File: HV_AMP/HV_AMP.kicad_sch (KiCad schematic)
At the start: 54 parts, among them K1 G5V-2, Q1 BC546, Q3 BC549, Q4 BC546, U1 4N35, U2 TL072, U3 TL072, U4 TL072, U5 LM7815_TO220, U6 LM7915_TO220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

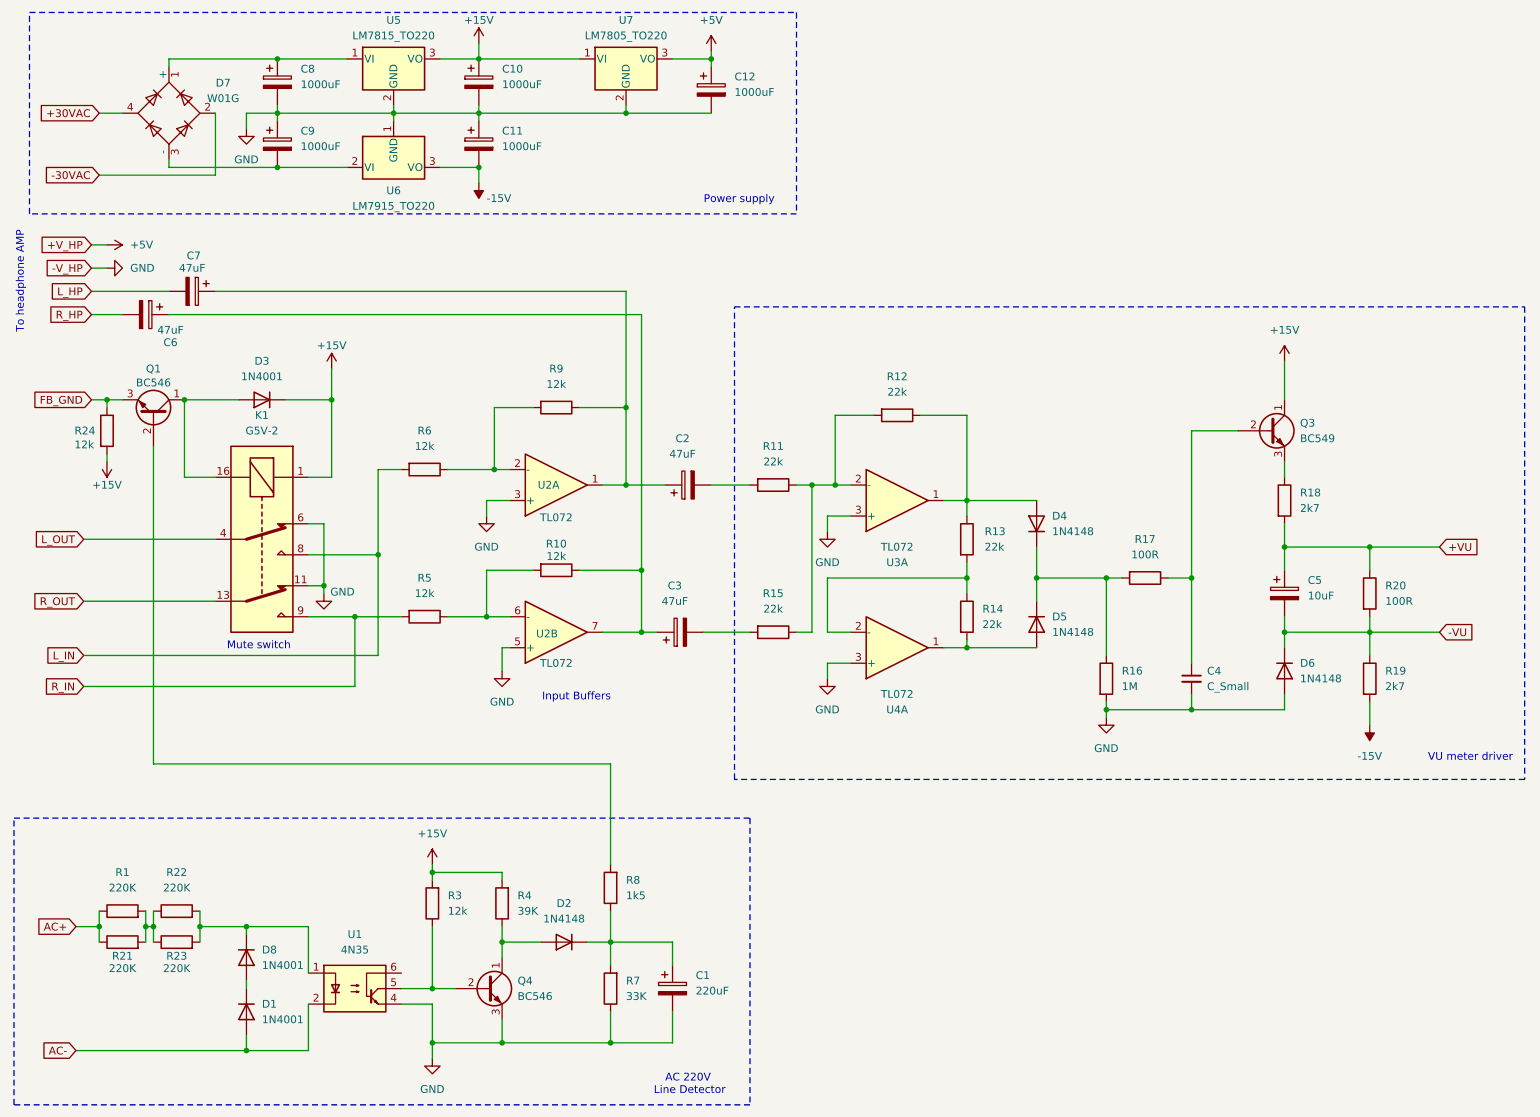
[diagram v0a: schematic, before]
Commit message: Fixing some circuit values for HV AMP
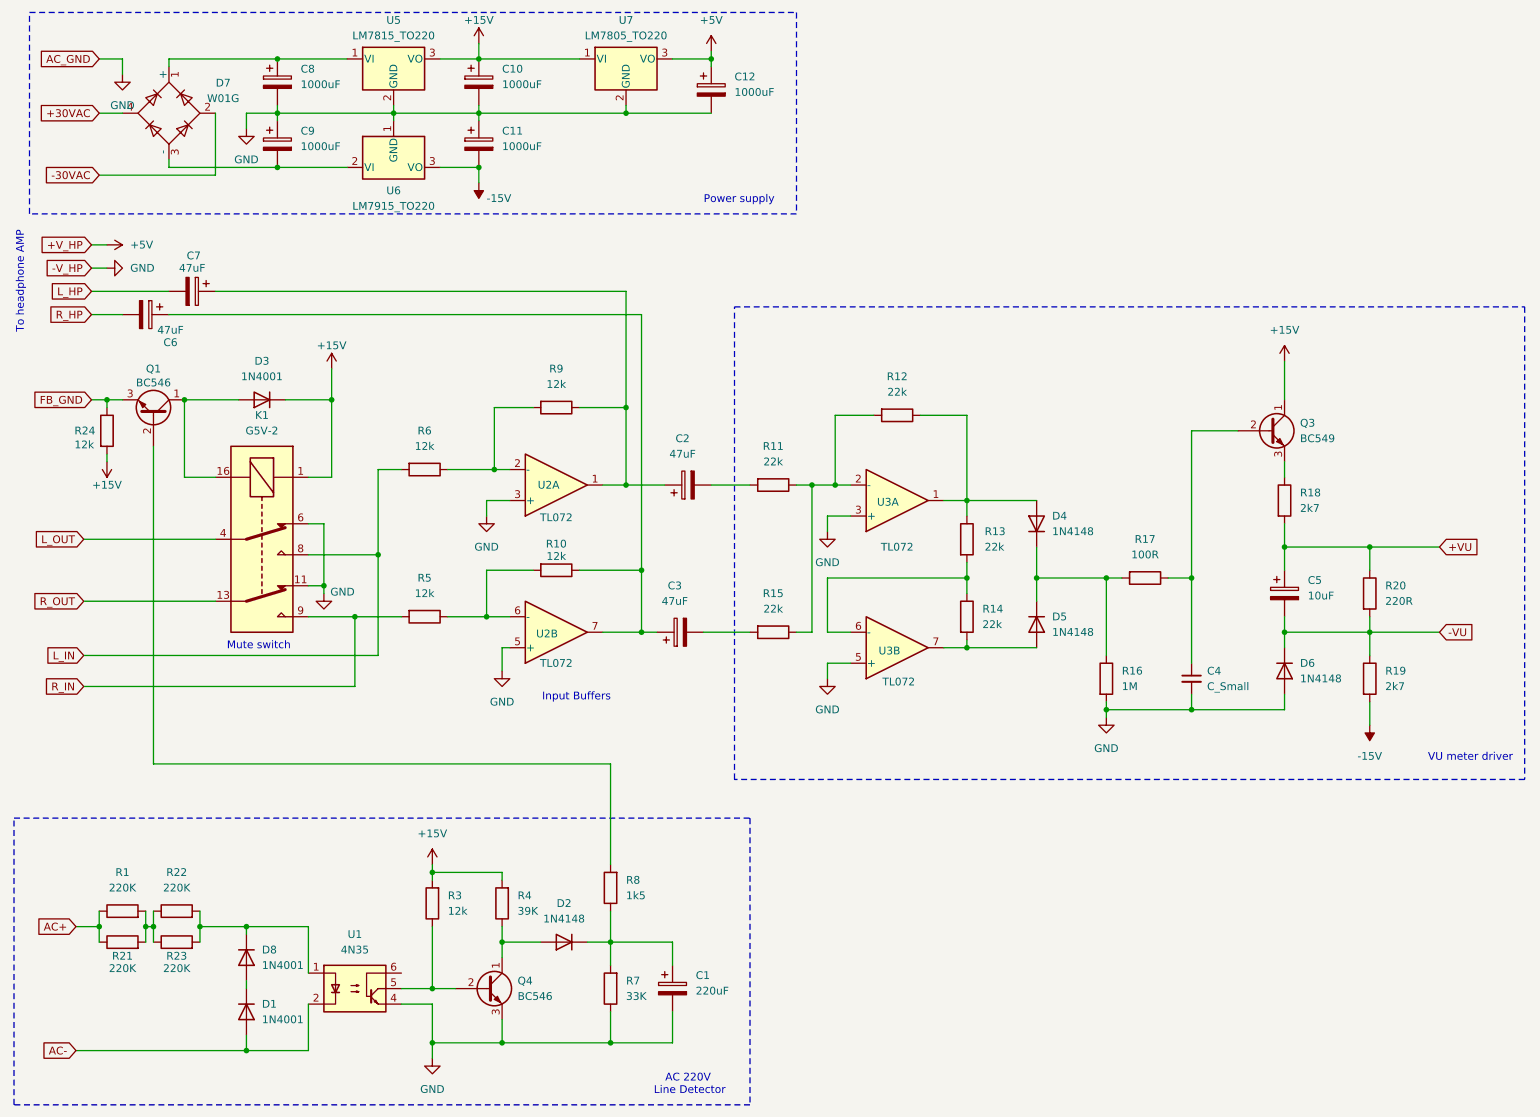
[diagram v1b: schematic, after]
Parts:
- R20: value 100R -> 220R
- renumbered U4 to U3
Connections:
- net GND: now also U3.5 (+); no longer U3.3 (+)
- net at D5.2 (A), R14.2: now also U3.7; no longer U3.1
- net at R13.2, R14.1: now also U3.6 (-); no longer U3.2 (-)
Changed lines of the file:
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@@
 	(wire
 		(pts
+			(xy 39.37 22.86) (xy 43.18 22.86)
+		)
+		(stroke
+			(width 0)
+			(type default)
+		)
+	)
+	(wire
+		(pts
 			(xy 39.37 41.91) (xy 58.42 41.91)
 		)
@@
 	(wire
 		(pts
+			(xy 43.18 22.86) (xy 43.18 25.4)
+		)
+		(stroke
+			(width 0)
+			(type default)
+		)
+	)
+	(wire
+		(pts
 			(xy 39.37 165.1) (xy 39.37 167.64)
 		)
@@
 		)
 	)
+	(global_label "AC_GND"
+		(shape input)
+		(at 39.37 22.86 180)
+		(fields_autoplaced yes)
+		(effects
+			(font
+				(size 1.27 1.27)
+			)
+			(justify right)
+		)
+		(property "Intersheetrefs" "${INTERSHEET_REFS}"
+			(at 29.1881 22.86 0)
+			(effects
+				(font
+					(size 1.27 1.27)
+				)
+				(justify right)
+				(hide yes)
+			)
+		)
+	)
 	(global_label "L_OUT"
 		(shape input)
@@
 		(dnp no)
 		(property "Reference" "U3"
-			(at 170.18 105.41 0)
+			(at 168.656 95.504 0)
 			(effects
 				(font
@@
 		(at 170.18 119.38 0)
 		(mirror x)
-		(unit 1)
+		(unit 2)
 		(exclude_from_sim no)
 		(in_bom yes)
 		(on_board yes)
 		(dnp no)
-		(property "Reference" "U4"
-			(at 170.18 129.54 0)
+		(property "Reference" "U3"
+			(at 168.91 119.888 0)
 			(effects
 				(font
@@
 		)
 		(property "Value" "TL072"
-			(at 170.18 127 0)
+			(at 170.434 124.968 0)
 			(effects
 				(font
@@
 			(project "HV_amp_circuits"
 				(path "/6567d1e3-e9e0-430a-8803-85c2ad7fe865"
-					(reference "U4")
-					(unit 1)
+					(reference "U3")
+					(unit 2)
 				)
 			)
@@
 	)
 	(symbol
+		(lib_id "power:GND")
+		(at 43.18 25.4 0)
+		(unit 1)
+		(exclude_from_sim no)
+		(in_bom yes)
+		(on_board yes)
+		(dnp no)
+		(fields_autoplaced yes)
+		(property "Reference" "#PWR019"
+			(at 43.18 31.75 0)
+			(effects
+				(font
+					(size 1.27 1.27)
+				)
+				(hide yes)
+			)
+		)
+		(property "Value" "GND"
+			(at 43.18 30.48 0)
+			(effects
+				(font
+					(size 1.27 1.27)
+				)
+			)
+		)
+		(property "Footprint" ""
+			(at 43.18 25.4 0)
+			(effects
+				(font
+					(size 1.27 1.27)
+				)
+				(hide yes)
+			)
+		)
+		(property "Datasheet" ""
+			(at 43.18 25.4 0)
+			(effects
+				(font
+					(size 1.27 1.27)
+				)
+				(hide yes)
+			)
+		)
+		(property "Description" "Power symbol creates a global label with name \"GND\" , ground"
+			(at 43.18 25.4 0)
+			(effects
+				(font
+					(size 1.27 1.27)
+				)
+				(hide yes)
+			)
+		)
+		(pin "1"
+		)
+		(instances
+			(project "HV_AMP"
+				(path "/6567d1e3-e9e0-430a-8803-85c2ad7fe865"
+					(reference "#PWR019")
+					(unit 1)
+				)
+			)
+		)
+	)
+	(symbol
 		(lib_id "Device:R")
 		(at 181.61 114.3 0)
@@
 			)
 		)
-		(property "Value" "100R"
+		(property "Value" "220R"
 			(at 250.19 111.7599 0)
 			(effects

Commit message: New circuits!
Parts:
- C10, C11: value 1000uF -> 1000uF X 25V
- C12: value 1000uF -> 1000uF X 10V
- C8, C9: value 1000uF -> 1000uF X 50V
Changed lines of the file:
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@@
 			)
 		)
-		(property "Value" "1000uF"
+		(property "Value" "1000uF X 25V"
 			(at 105.41 37.2109 0)
 			(effects
@@
 		(on_board yes)
 		(dnp no)
-		(fields_autoplaced yes)
 		(property "Reference" "C9"
 			(at 72.39 34.6709 0)
@@
 			)
 		)
-		(property "Value" "1000uF"
-			(at 72.39 37.2109 0)
+		(property "Value" "1000uF X 50V"
+			(at 66.04 42.418 0)
 			(effects
 				(font
@@
 			)
 		)
-		(property "Value" "1000uF"
+		(property "Value" "1000uF X 10V"
 			(at 143.51 28.3209 0)
 			(effects
@@
 		(on_board yes)
 		(dnp no)
-		(fields_autoplaced yes)
 		(property "Reference" "C8"
 			(at 72.39 24.5109 0)
@@
 			)
 		)
-		(property "Value" "1000uF"
-			(at 72.39 27.0509 0)
+		(property "Value" "1000uF X 50V"
+			(at 69.342 29.21 0)
 			(effects
 				(font
@@
 			)
 		)
-		(property "Value" "1000uF"
+		(property "Value" "1000uF X 25V"
 			(at 105.41 27.0509 0)
 			(effects
